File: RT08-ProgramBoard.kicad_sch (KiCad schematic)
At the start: 9 parts, among them J1 PWR/Addr, J2 Inst-1, J3 Inst-2, J4 Data-1, J5 Data-2, J6 Inst-1, J7 Inst-2, J8 Data-1, J9 Data-2

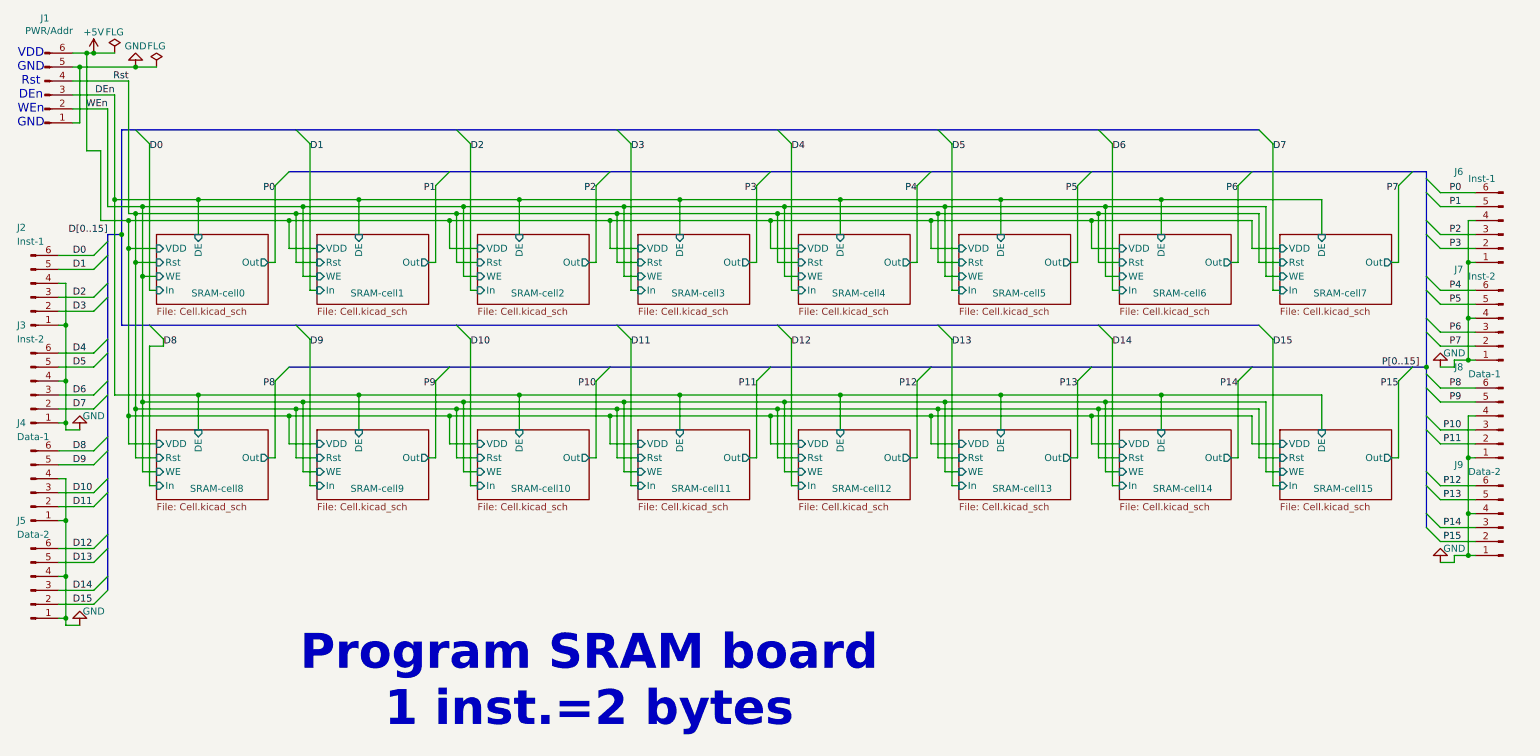
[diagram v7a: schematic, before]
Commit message: Merged In/Out pins to one pin groups!
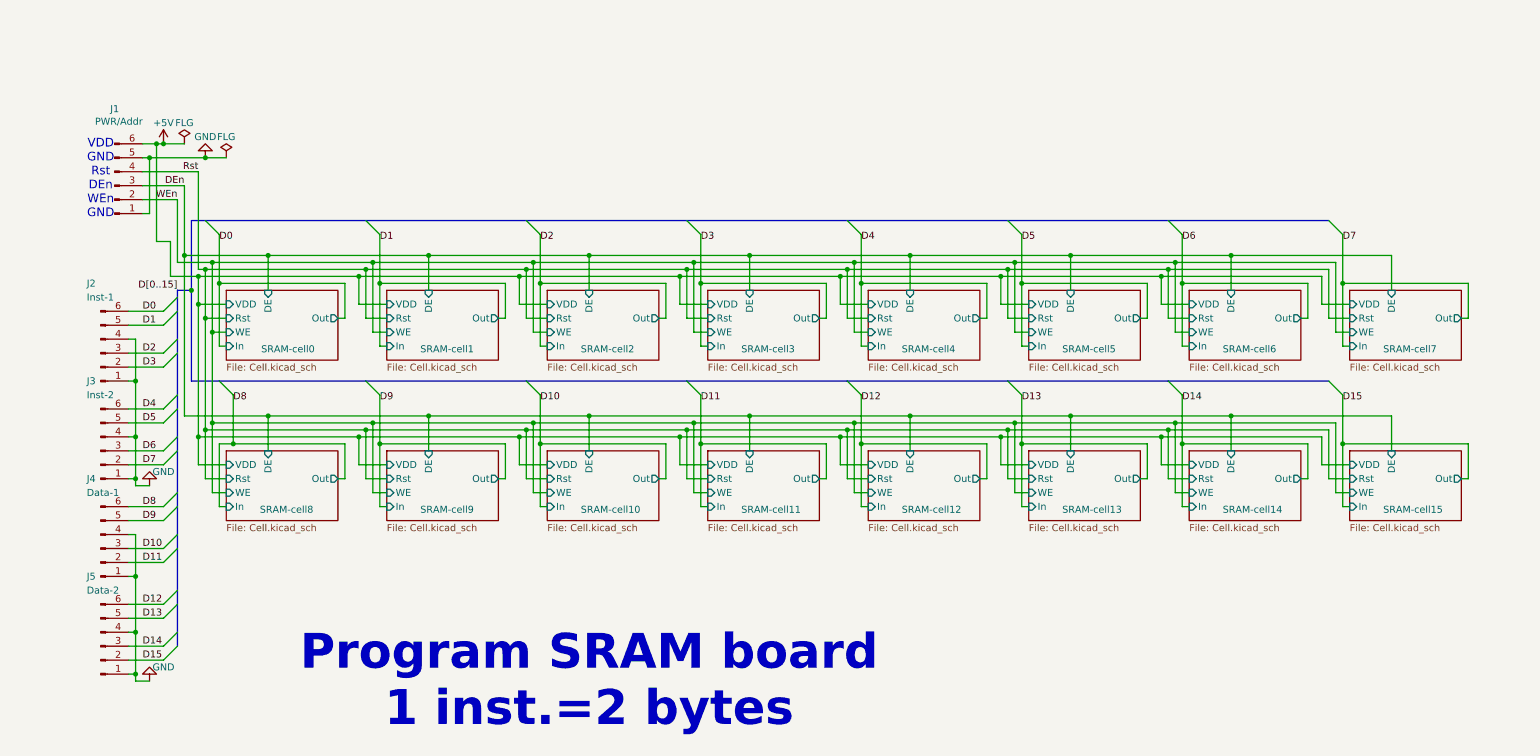
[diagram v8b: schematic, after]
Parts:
- removed J6: Inst-1, Connector_PinHeader_2.54mm:PinHeader_1x06_P2.54mm_Vertical, symbol Connector:Conn_01x06_Pin
- removed J7: Inst-2, Connector_PinHeader_2.54mm:PinHeader_1x06_P2.54mm_Vertical, symbol Connector:Conn_01x06_Pin
- removed J8: Data-1, Connector_PinHeader_2.54mm:PinHeader_1x06_P2.54mm_Vertical, symbol Connector:Conn_01x06_Pin
- removed J9: Data-2, Connector_PinHeader_2.54mm:PinHeader_1x06_P2.54mm_Vertical, symbol Connector:Conn_01x06_Pin
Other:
- moved on the sheet: J1, J2, J3, J4, J5
